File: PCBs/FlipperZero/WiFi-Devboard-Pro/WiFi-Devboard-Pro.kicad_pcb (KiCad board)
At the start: 2 copper layers, 78.5 x 20.1 mm, 46 parts, among them IC1 ESP32-WROOM-32E-N4, IC2 DMP1045U-7, IC3 AZ1117H-3.3TRE1, IC4 DMP1045U-7, IC5 DMP1045U-7, J1 3220-10-0300-00, J2 X6511WVS-08H-C60D48R2, J3 DZ254S-11-10-48, J4 Conn_01x11, J5 Conn_01x11, J6 503398-1892, U1 MMDT2907A-7-F, U2 MMDT2907A-7-F, U3 MMDT2907A-7-F

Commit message: push conflict resolve
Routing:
- net +ext_3V3: track 44.6 -> 41.1 mm
- net Net-(IC4-Pad1): track 12.2 -> 9.64 mm
- net +3V3: track 42.0 -> 43.9 mm, vias 23 -> 15
- net +ext_5V: track 47.2 -> 46.1 mm
- net +5V: track 34.7 -> 34.2 mm

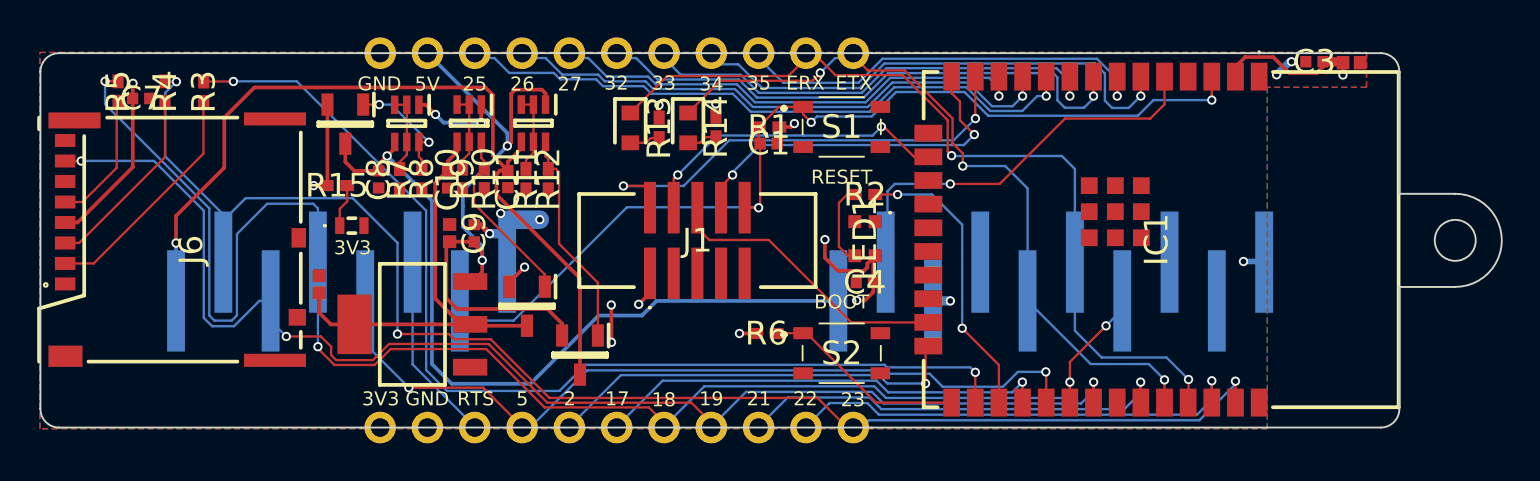
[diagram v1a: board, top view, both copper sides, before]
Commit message: Stream review, add logo and text
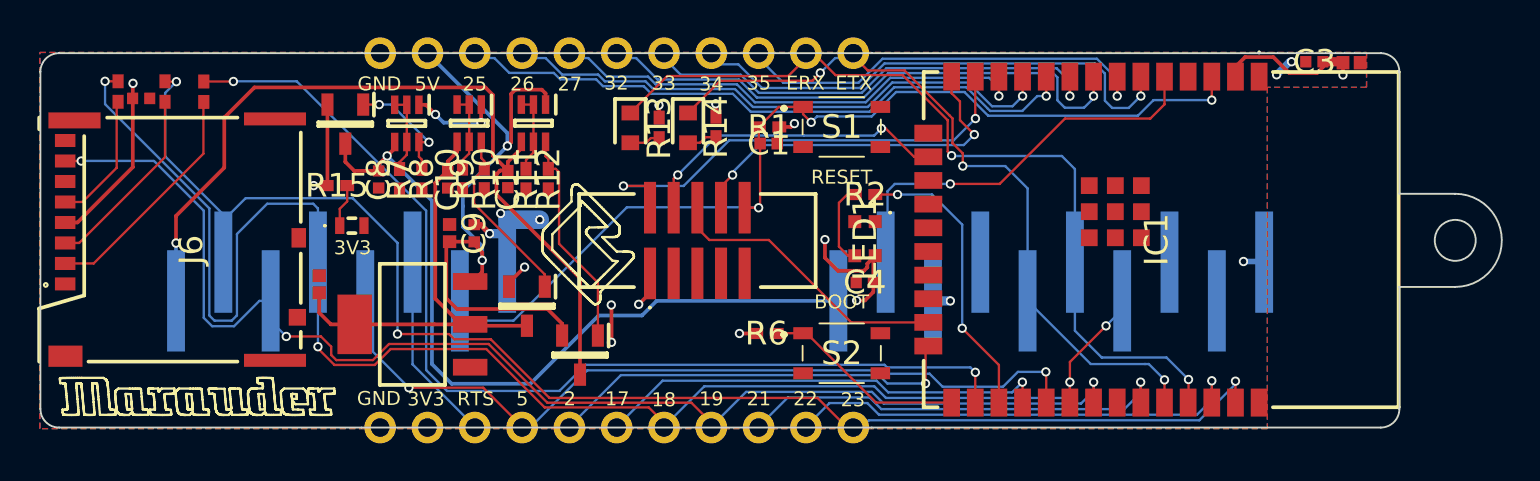
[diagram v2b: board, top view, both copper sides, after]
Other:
- board text added: "Flipper Zero WiFi Devboard Pro Rev V0.1.0 JustCallMeKoko & trisp3ar"

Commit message: Place drill hole, fill graphics, remove fab marks
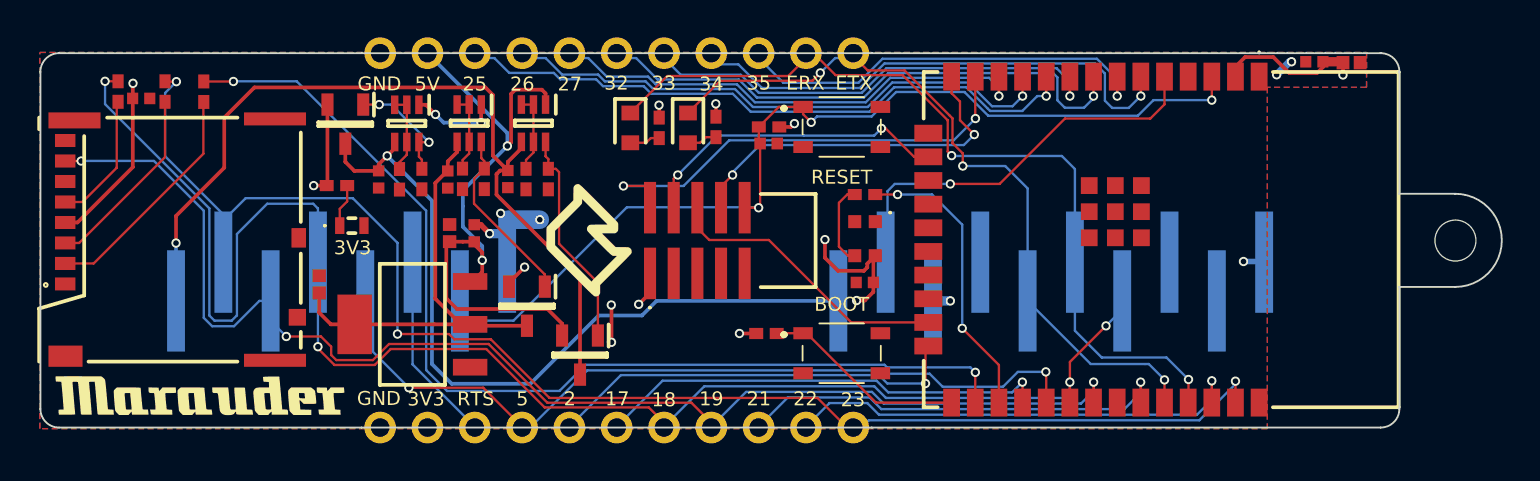
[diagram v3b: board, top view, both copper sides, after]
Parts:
- added ?: , , F.Cu at (187.1, 99.9)
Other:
- outline, holes or cut-outs redrawn
